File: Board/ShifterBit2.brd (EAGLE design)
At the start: 27.2 x 51.2 mm, 18 parts, among them J1 HIROSE_DM3CS-SF, U1 LV321SOT23-5, U2 LV321SOT23-5

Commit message: removed esd protection
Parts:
- removed C1: 0.1uF, LITTLEBITS:CAP-0603
- removed C2: 10uF, LITTLEBITS:CAP-0603
- removed C3: 1.0uF, LITTLEBITS:CAP-0603
- removed FB1: FERRITE-BEAD0603, LITTLEBITS:R0603
- removed R2: 10K, LITTLEBITS:RES-0603
- removed R3, R4: 3K3, LITTLEBITS:RES-0603
- removed TVS1, TVS2: ESD9B5.0ST5G, LITTLEBITS:SOD-923
- removed U$5: FRAME-LETTER-OHWOHW, LITTLEBITS:FABDWG01-OHW
- removed U1, U2: LV321SOT23-5, LITTLEBITS:SOT23-5
- moved R1 2.21 mm to (13.2, 53.1)
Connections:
- removed net LB_VCC: BSF1.VCC, BSM1.VCC1, FB1.2
- removed net N$2: U1.3, U1.4
- removed net N$3: U2.1
- removed net N$4: R2.1, U1.1
- removed net VREF: C2.1, R3.1, R4.2
- new net SIG: R1.2
- net GND: no longer C1.2, C2.2, C3.1, R4.1, TVS1.1, TVS2.1, U1.2, U2.2
- net SIG_IN: no longer R1.2, R2.2, TVS1.2
- net SIG_OUT: no longer TVS2.2, U2.3, U2.4
- net VCC: now also BSF1.VCC, BSM1.VCC1; no longer C1.1, C3.2, FB1.1, R3.2, U1.5, U2.5
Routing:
- net LB_VCC: track 58.2 -> 0.00 mm
- net VCC: track 50.1 -> 0.00 mm, vias 2 -> 0
- net N$4: track 6.28 -> 0.00 mm
- net SIG_OUT: track 5.43 -> 0.00 mm
- net SIG_IN: track 4.90 -> 0.00 mm
- net VREF: track 4.85 -> 0.00 mm
- net N$2: track 4.15 -> 0.00 mm

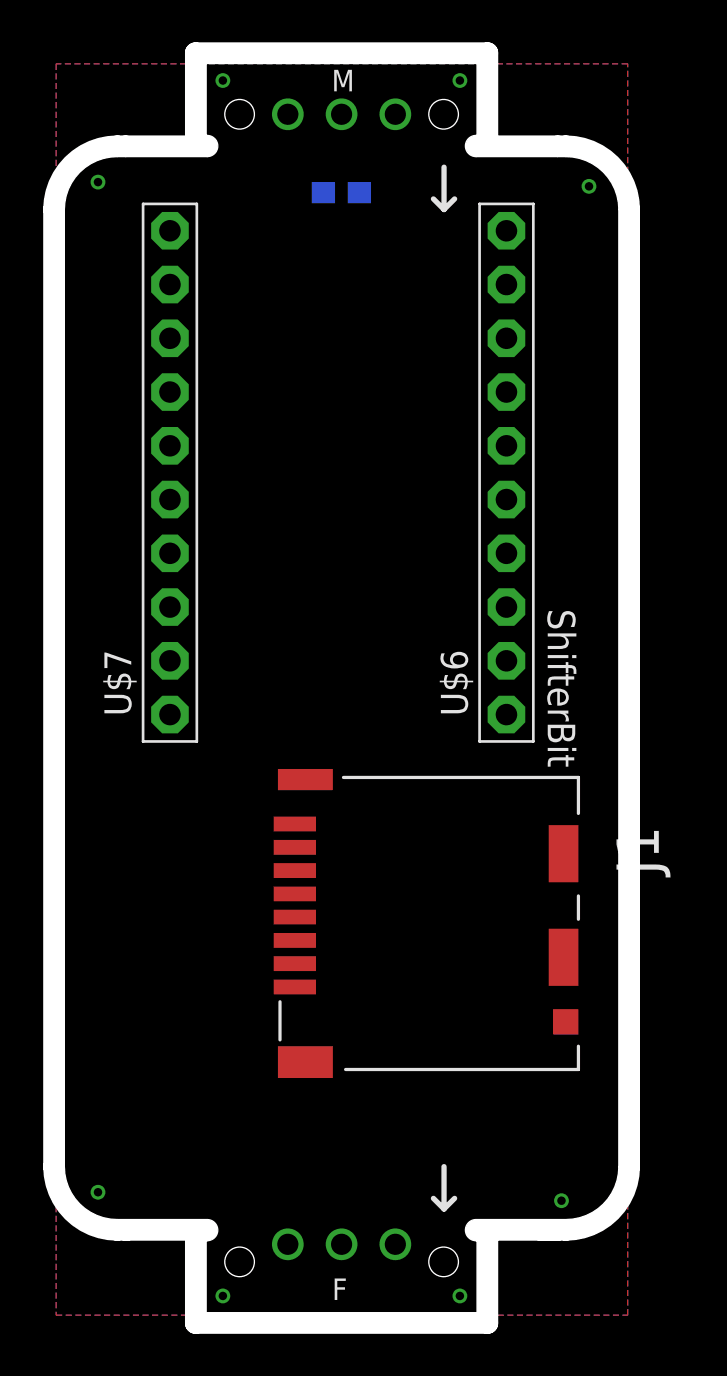
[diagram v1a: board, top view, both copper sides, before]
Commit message: added nets and leds
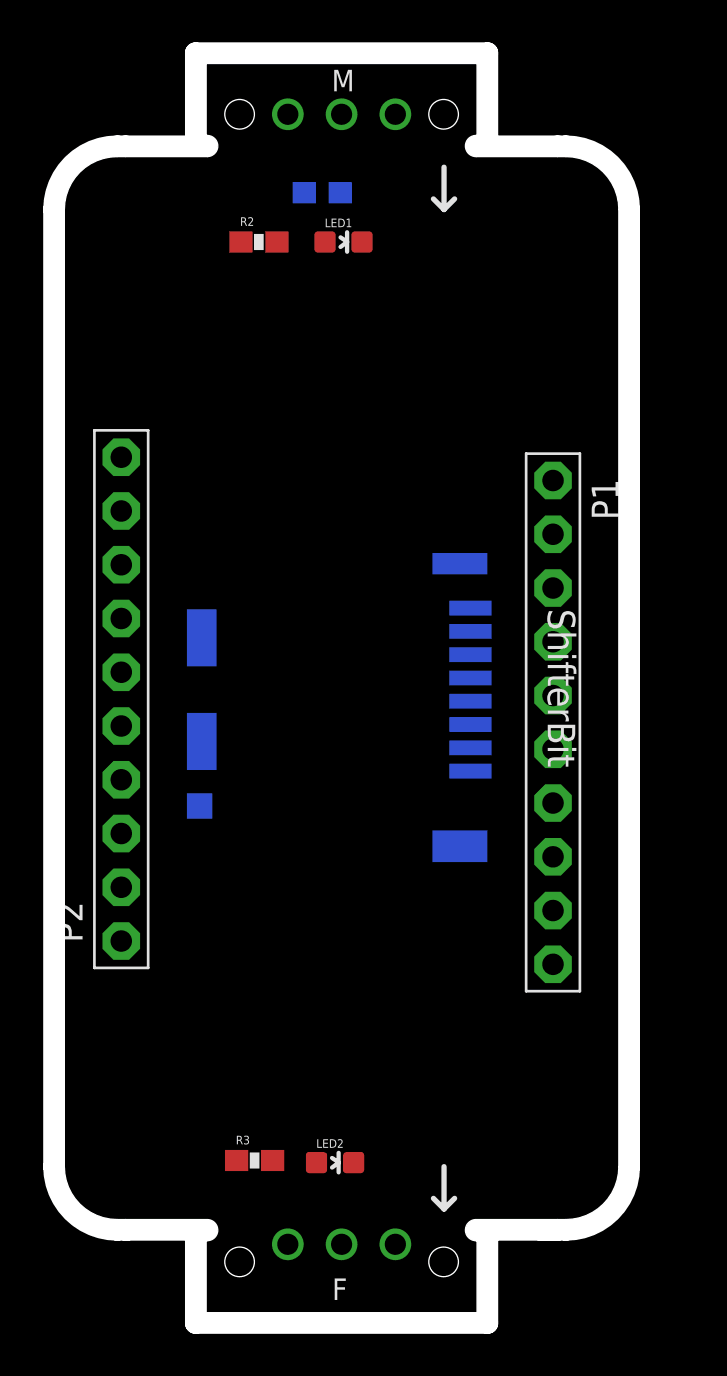
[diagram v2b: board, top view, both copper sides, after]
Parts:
- removed J1: HIROSE_DM3CS-SF, HIROSE-DM3CS-SF:HIROSE_DM3CS-SF
- removed U$6, U$7: PINHD-1X10, adafruit:1X10-BIG
- added LED1, LED2: (no value), SparkFun-LED:LED-0603
- added P1, P2: (no value), adafruit:1X10-BIG
- added R2, R3: 56, SparkFun-Passives:0603-RES
- added SD1: (no value), HIROSE-DM3CS-SF:HIROSE_DM3CS-SF
- R1: value 1meg -> 1M
- moved R1 0.90 mm to (12.3, 53.1)
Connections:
- removed net SIG: R1.2
- new net 3V: P2.3
- new net A: P1.2
- new net D0: P2.6
- new net D12: P1.6
- new net D13: P1.7
- new net D14: P1.5
- new net D15: P2.4
- new net D16: P1.4
- new net D2: P2.5
- new net D4: P2.7, R3.1
- new net D5: P2.8, R2.1
- new net EN: P1.3
- new net LD0: P2.2
- new net N$1: SD1.5
- new net N$11: SD1.2
- new net N$12: SD1.1
- new net N$2: SD1.3
- new net N$3: SD1.4
- new net N$4: LED1.A, R2.2
- new net N$5: SD1.6
- new net N$6: SD1.7
- new net N$7: SD1.8
- new net N$8: SD1.11
- new net N$9: LED2.A, R3.2
- new net RST: P1.1
- new net RX: P2.9
- new net TX: P2.10
- new net V+: P1.8
- new net VBAT: P1.9
- net GND: now also LED1.C, LED2.C, P1.10, P2.1, SD1.10, SD1.12, SD1.13, SD1.9
- net SIG_IN: now also R1.2
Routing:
- removed copper zone on layer 1, net GND
- removed copper zone on layer 16, net GND
